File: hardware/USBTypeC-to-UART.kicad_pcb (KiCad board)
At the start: 2 copper layers, 28.2 x 17.5 mm, 5 parts, among them J1 USB-C, J2 Header, U1 CP2102N

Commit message: layout
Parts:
- added 0.1uf1: C, Capacitor_SMD:C_0805_2012Metric, F.Cu at (118.9, 124.7)
- added 0.1uf2: C, Capacitor_SMD:C_0805_2012Metric, F.Cu at (126.0, 111.3)
- added 1K1: R, Resistor_SMD:R_0805_2012Metric_Pad1.15x1.40mm_HandSolder, F.Cu at (123.7, 111.8)
- added 4.7uf1: C, Capacitor_SMD:C_1206_3216Metric, F.Cu at (119.3, 122.2)
- added 4.7uf2: C, Capacitor_SMD:C_1206_3216Metric, F.Cu at (121.2, 111.6)
- added 470R1: R, Resistor_SMD:R_0805_2012Metric_Pad1.15x1.40mm_HandSolder, F.Cu at (130.8, 121.9)
- added D1: SP0503BAHTG, digikey-footprints:SOT-143-4, F.Cu at (119.4, 116.1)
- added D2: LED, LED_SMD:LED_0805_2012Metric_Castellated, F.Cu at (129.8, 125.0)
- J1: value USB-C -> USB_C
- U1: value CP2102N -> CP2102N-A01-GQFN24
- moved 22K1 10.4 mm to (119.1, 119.9), turned to 0 degrees
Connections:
- U1 pad 15: (no net) -> /SUSPENDn
- U1 pad 9: (no net) -> Net-(1K1-Pad2)
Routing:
- net GND: track 4.01 -> 43.7 mm, vias 2 -> 3
- net /VBUS: track 6.35 -> 25.8 mm
- net VDD: track 14.8 -> 32.9 mm, vias 0 -> 3
- net Net-(1K1-Pad2): track 0.00 -> 14.5 mm, vias 0 -> 2
- net /D+: track 5.53 -> 14.4 mm
- net Net-(22K1-Pad2): track 2.01 -> 9.63 mm, vias 0 -> 2
- net /D-: track 5.47 -> 12.7 mm
- net /SUSPENDn: track 0.00 -> 4.08 mm
- net Net-(470R1-Pad2): track 0.00 -> 2.05 mm

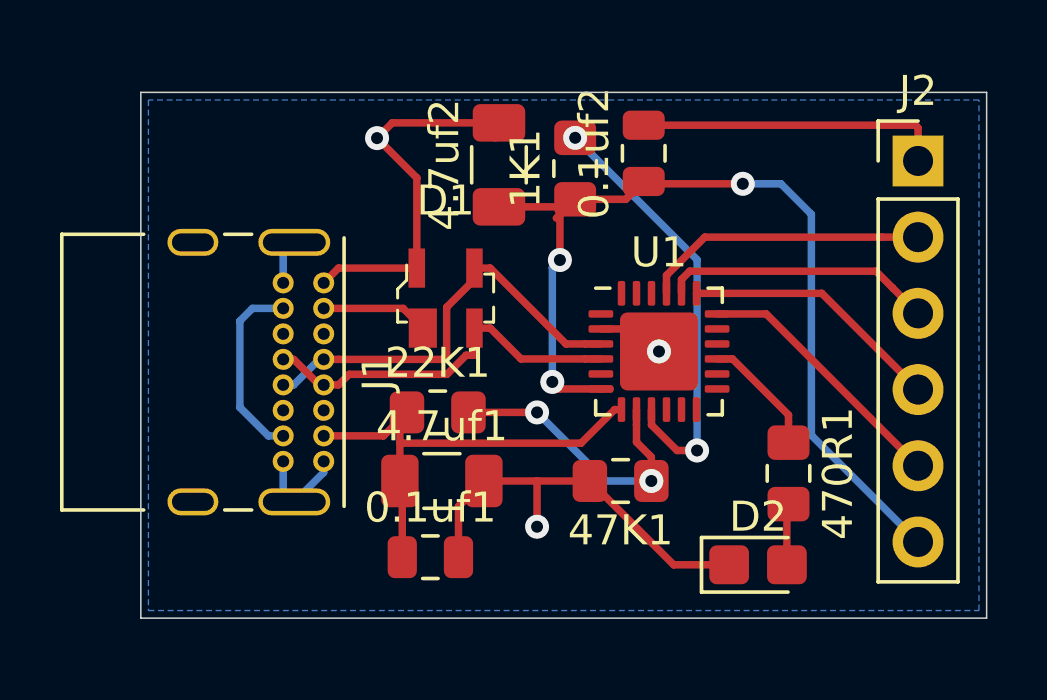
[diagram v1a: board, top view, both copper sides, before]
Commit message: usb connector 3d model
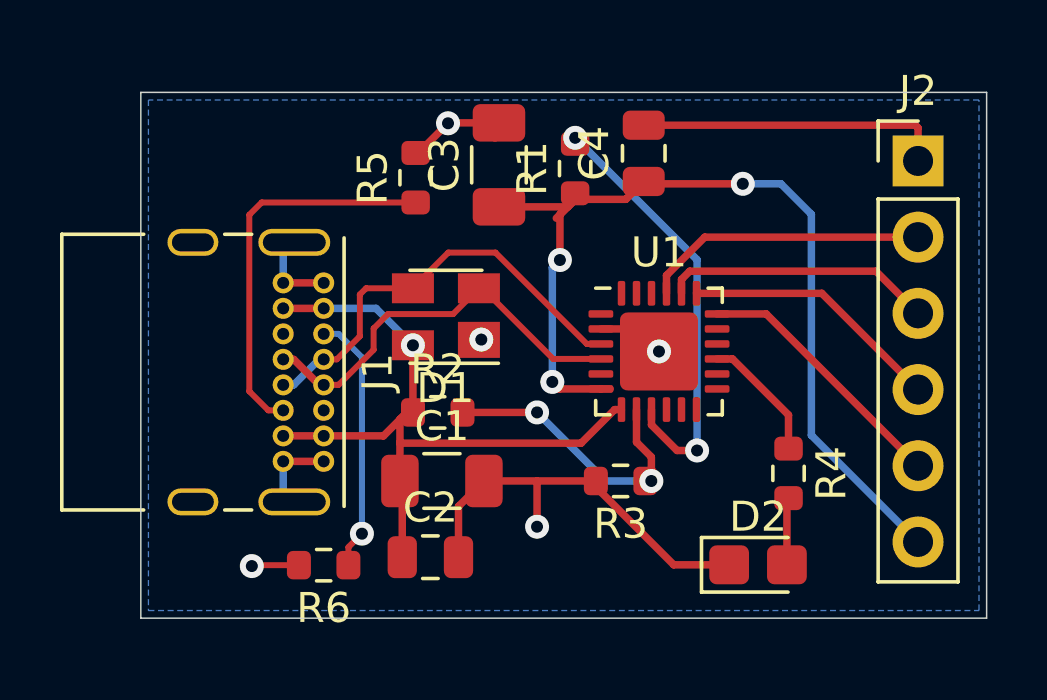
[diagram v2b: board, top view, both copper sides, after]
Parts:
- removed 1K1, 22K1, 470R1, 47K1: R, Resistor_SMD:R_0805_2012Metric_Pad1.15x1.40mm_HandSolder
- added R1: 1.1K, Resistor_SMD:R_0603_1608Metric, F.Cu at (123.7, 111.8)
- added R2: 22K, Resistor_SMD:R_0603_1608Metric, F.Cu at (119.1, 119.9)
- added R3: 47K, Resistor_SMD:R_0603_1608Metric, F.Cu at (125.2, 122.2)
- added R4: 220, Resistor_SMD:R_0603_1608Metric, F.Cu at (130.8, 121.9)
- added R5: 5.1K, Resistor_SMD:R_0603_1608Metric, F.Cu at (118.4, 112.1)
- added R6: 5.1K, Resistor_SMD:R_0603_1608Metric, F.Cu at (115.3, 125.0)
- C1: renamed from 4.7uf1; value C -> 4.7uf
- C2: renamed from 0.1uf1; value C -> 100nf
- C3: renamed from 4.7uf2; value C -> 4.7uf
- C4: renamed from 0.1uf2; value C -> 100nf
- D1: footprint digikey-footprints:SOT-143-4 -> Package_TO_SOT_SMD:SOT-143
- J1: value USB_C -> USB_C_Receptacle_USB2.0
- J2: value Header -> Conn_01x06_Male
- moved D1 0.62 mm to (119.4, 116.7), turned to 180 degrees
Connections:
- D1 pad 2: /VBUS -> /D-
- D1 pad 3: /D- -> /D+
- D1 pad 4: /D+ -> /VBUS
- J1 pad A5: (no net) -> Net-(J1-PadA5)
- J1 pad B5: (no net) -> Net-(J1-PadB5)
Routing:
- net Net-(J1-PadB5): track 0.00 -> 13.0 mm
- net Net-(J1-PadA5): track 0.00 -> 8.71 mm, vias 0 -> 1
- net GND: track 43.7 -> 36.9 mm, vias 3 -> 5
- net /VBUS: track 25.8 -> 24.3 mm, vias 0 -> 1
- net /D-: track 12.7 -> 13.7 mm
